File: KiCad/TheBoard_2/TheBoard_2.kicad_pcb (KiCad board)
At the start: 2 copper layers, 150 x 100 mm, 9 parts, among them J1 Conn_01x03_Female, J2 Conn_01x03_Female, J3 Conn_01x16_Female, J4 Conn_01x32_Male, J5 Conn_01x16_Female

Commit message: Adding ground to output pins
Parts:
- J4: value Conn_01x32_Male -> Conn_01x36_Male; footprint Connector_PinHeader_2.54mm:PinHeader_1x32_P2.54mm_Horizontal -> Connector_PinHeader_2.54mm:PinHeader_2x18_P2.54mm_Horizontal
- moved J4 19.8 mm to (176.5, 140.3)
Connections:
- J4 pad 1: unconnected-(J4-Pad1) -> GND
- J4 pad 2: unconnected-(J4-Pad2) -> GND

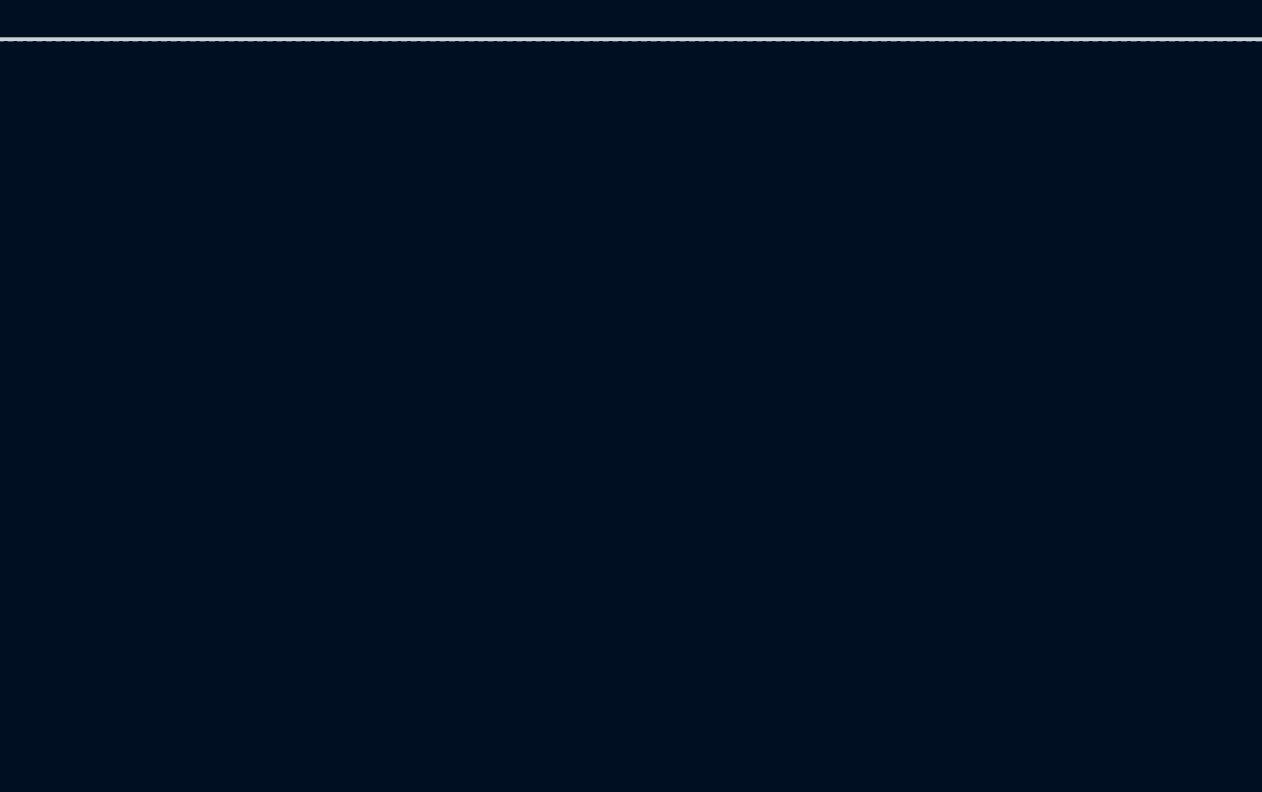
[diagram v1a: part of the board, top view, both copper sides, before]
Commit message: Adding -5V circuit
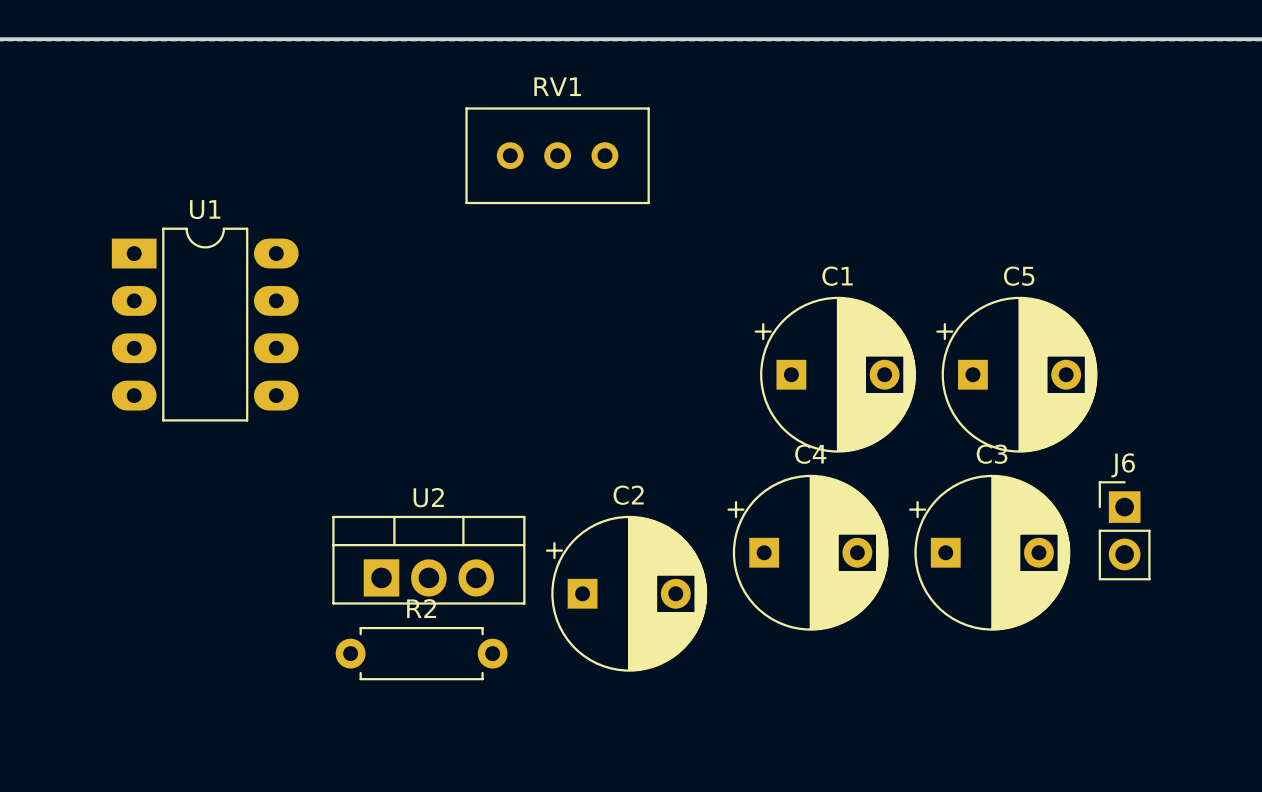
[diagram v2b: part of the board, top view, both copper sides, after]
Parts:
- added C1: C, Capacitor_THT:CP_Radial_D8.0mm_P5.00mm, F.Cu at (159.8, 65.2)
- added C2: C, Capacitor_THT:CP_Radial_D8.0mm_P5.00mm, F.Cu at (148.6, 77.0)
- added C3: C, Capacitor_THT:CP_Radial_D8.0mm_P5.00mm, F.Cu at (168.0, 74.8)
- added C4: C, Capacitor_THT:CP_Radial_D8.0mm_P5.00mm, F.Cu at (158.3, 74.8)
- added C5: C, Capacitor_THT:CP_Radial_D8.0mm_P5.00mm, F.Cu at (169.5, 65.2)
- added J6: Conn_01x02_Male, Connector_PinHeader_2.54mm:PinHeader_1x02_P2.54mm_Vertical, F.Cu at (177.6, 72.3)
- added R2: R, Resistor_THT:R_Axial_DIN0207_L6.3mm_D2.5mm_P7.62mm_Horizontal, F.Cu at (136.1, 80.2)
- added RV1: R_Potentiometer_Trim, Potentiometer_THT:Potentiometer_Bourns_3296W_Vertical, F.Cu at (149.8, 53.5)
- added U1: MAX680CSA+T, Package_DIP:DIP-8_W7.62mm_LongPads, F.Cu at (124.5, 58.8)
- added U2: LM337_TO220, Package_TO_SOT_THT:TO-220-3_Vertical, F.Cu at (137.8, 76.2)

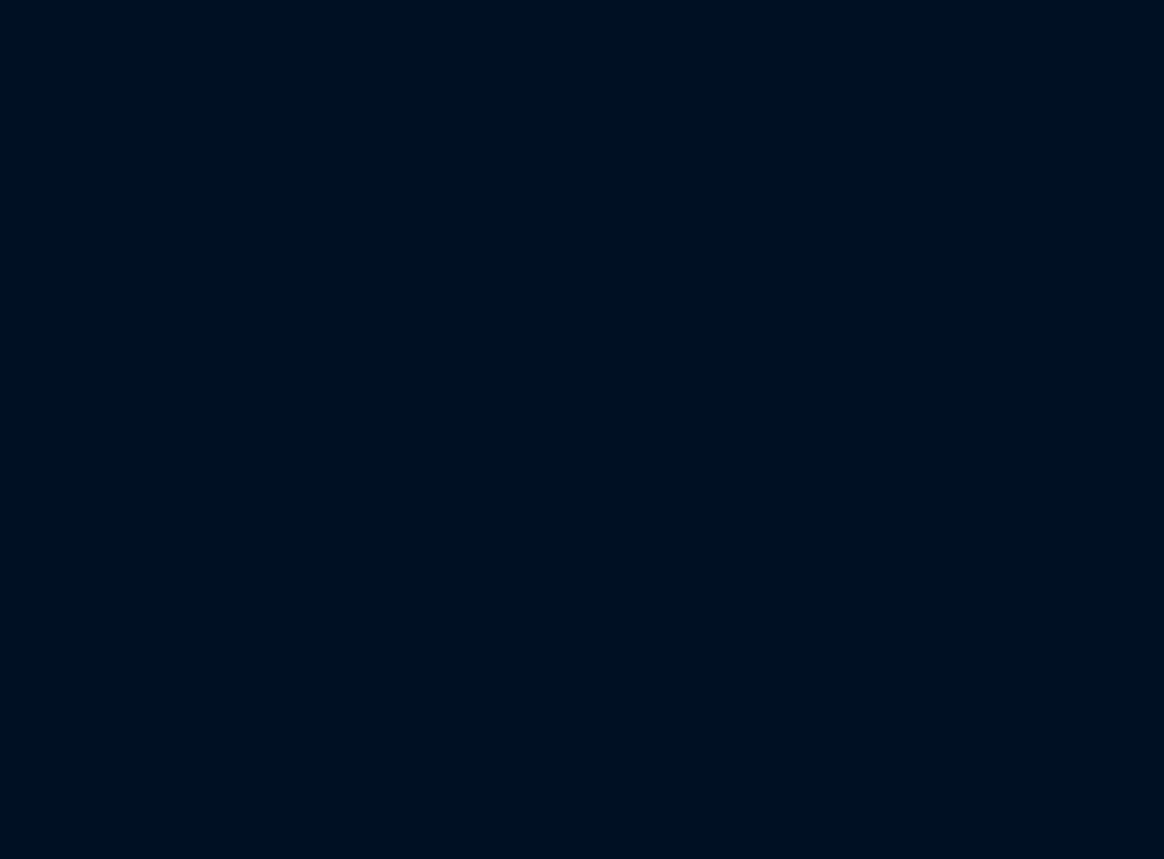
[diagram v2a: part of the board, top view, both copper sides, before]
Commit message: adding mt3608 circuit
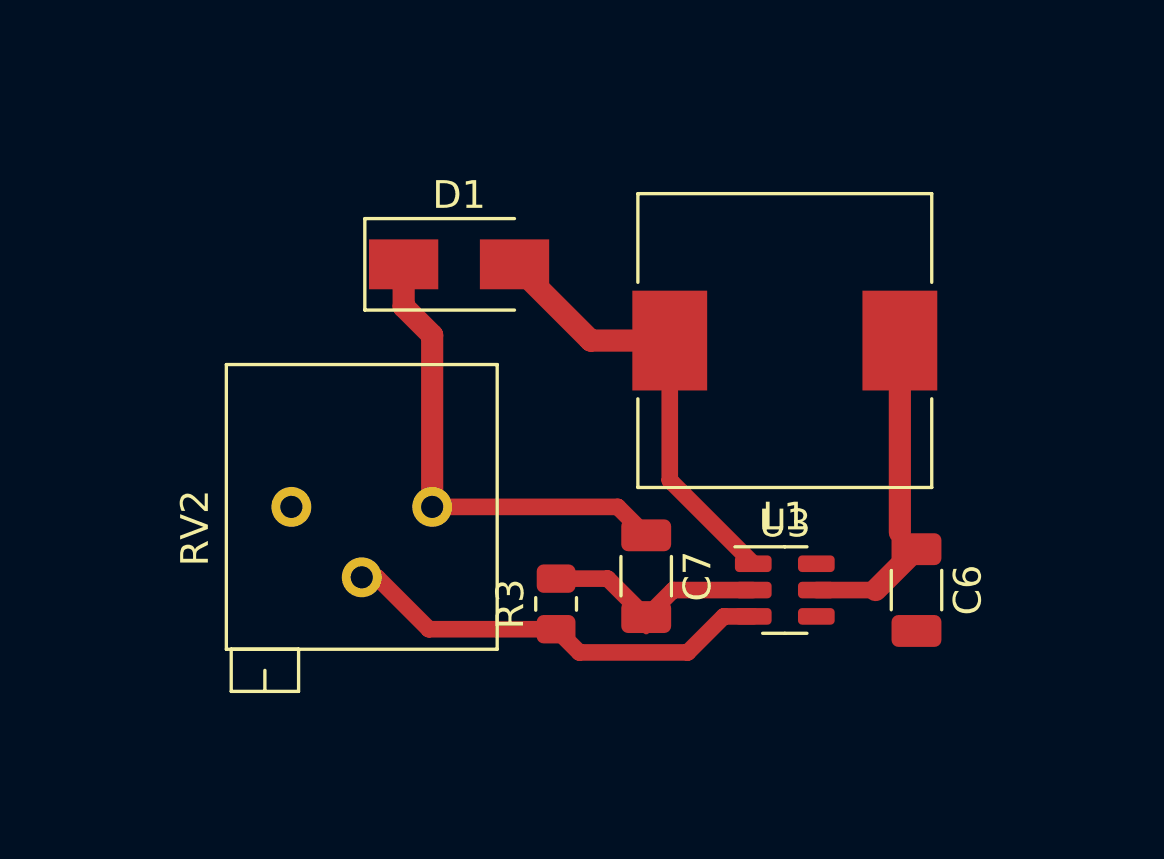
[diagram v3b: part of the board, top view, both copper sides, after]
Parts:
- added C6: C, Capacitor_SMD:C_1206_3216Metric, F.Cu at (134.0, 121.0)
- added C7: C, Capacitor_SMD:C_1206_3216Metric, F.Cu at (124.2, 120.5)
- added D1: D, Diode_SMD:D_SMA, F.Cu at (117.5, 109.2)
- added L1: L, Inductor_SMD:L_10.4x10.4_H4.8, F.Cu at (129.2, 112.0)
- added R3: R, Resistor_SMD:R_0805_2012Metric, F.Cu at (121.0, 121.5)
- added RV2: R_Potentiometer, Potentiometer_THT:Potentiometer_Bourns_3296P_Horizontal, F.Cu at (111.5, 118.0)
- added U3: MT3608, Package_TO_SOT_SMD:SOT-23-6, F.Cu at (129.2, 121.0)
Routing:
- net Net-(D1-Pad1): track 0.00 -> 17.3 mm
- net Net-(D1-Pad2): track 0.00 -> 16.0 mm
- net Net-(U3-Pad3): track 0.00 -> 15.8 mm
- net Net-(C6-Pad1): track 0.00 -> 12.0 mm
- net GND: track 0.00 -> 8.25 mm

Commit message: Adding battery circuit
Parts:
- added C10: C, Capacitor_SMD:C_0603_1608Metric_Pad1.08x0.95mm_HandSolder, F.Cu at (115.9, 112.3)
- added C8: C, Capacitor_SMD:C_0402_1005Metric_Pad0.74x0.62mm_HandSolder, F.Cu at (107.9, 114.1)
- added C9: C, Capacitor_SMD:C_0402_1005Metric_Pad0.74x0.62mm_HandSolder, F.Cu at (115.9, 108.4)
- added D2: LED, LED_SMD:LED_0402_1005Metric_Pad0.77x0.64mm_HandSolder, F.Cu at (110.7, 105.4)
- added D3: LED, LED_SMD:LED_0402_1005Metric_Pad0.77x0.64mm_HandSolder, F.Cu at (112.2, 105.4)
- added J7: USB_B_Micro, Connector_USB:USB_Micro-B_Molex_47346-0001, F.Cu at (102.4, 111.6)
- added Q1: FS8205A, Package_SO:TSSOP-8_4.4x3mm_P0.65mm, F.Cu at (120.7, 115.3)
- added R1: R, Resistor_SMD:R_0402_1005Metric_Pad0.72x0.64mm_HandSolder, F.Cu at (110.7, 107.9)
- added R4: R, Resistor_SMD:R_0402_1005Metric_Pad0.72x0.64mm_HandSolder, F.Cu at (112.2, 107.9)
- added R5: R, Resistor_SMD:R_0402_1005Metric_Pad0.72x0.64mm_HandSolder, F.Cu at (110.4, 118.6)
- added R6: R, Resistor_SMD:R_0402_1005Metric_Pad0.72x0.64mm_HandSolder, F.Cu at (115.9, 116.1)
- added R7: R, Resistor_SMD:R_0402_1005Metric_Pad0.72x0.64mm_HandSolder, F.Cu at (115.9, 105.8)
- added U4: TP4056, Package_SO:SOIC-8-1EP_3.9x4.9mm_P1.27mm_EP2.29x3mm, F.Cu at (111.7, 114.1)
- added U5: DW01, Package_TO_SOT_SMD:SOT-23-6_Handsoldering, F.Cu at (120.7, 108.1)
- moved C1 27.0 mm to (186.7, 64.5)
- moved C2 27.0 mm to (175.5, 76.2)
- moved C3 27.0 mm to (195.0, 74.0)
- moved C4 27.0 mm to (185.3, 74.0)
- moved C5 27.0 mm to (196.5, 64.5)
- moved J6 27.0 mm to (204.6, 71.5)
- moved R2 27.0 mm to (163.1, 79.4)
- moved RV1 27.0 mm to (176.7, 52.7)
- moved U1 27.0 mm to (151.5, 58.0)
- moved U2 27.0 mm to (164.7, 75.3)
- moved C6 19.5 mm to (153.2, 117.2)
- moved C7 19.5 mm to (143.4, 116.7)
- moved D1 19.5 mm to (136.7, 105.5)
- moved L1 19.5 mm to (148.4, 108.2)
- moved R3 19.5 mm to (140.2, 117.7)
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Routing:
- net GND: track 8.25 -> 41.3 mm
- net Net-(C8-Pad1): track 0.00 -> 29.5 mm, vias 0 -> 2
- net B-: track 0.00 -> 15.1 mm
- net unconnected-(J7-Pad6): track 0.00 -> 12.6 mm
- net OUT/B+: track 0.00 -> 10.7 mm
- net Net-(U5-Pad3): track 0.00 -> 9.62 mm, vias 0 -> 2
- net Net-(U5-Pad2): track 0.00 -> 8.22 mm, vias 0 -> 2
- net Net-(C9-Pad1): track 0.00 -> 8.12 mm
- net Net-(Q1-Pad1): track 0.00 -> 5.74 mm
- net Net-(R1-Pad2): track 0.00 -> 3.23 mm
- net Net-(R4-Pad2): track 0.00 -> 3.14 mm
- net Net-(U5-Pad1): track 0.00 -> 3.05 mm
- net Net-(R5-Pad1): track 0.00 -> 2.03 mm
- net Net-(D3-Pad1): track 0.00 -> 1.33 mm
- net Net-(D2-Pad1): track 0.00 -> 1.33 mm

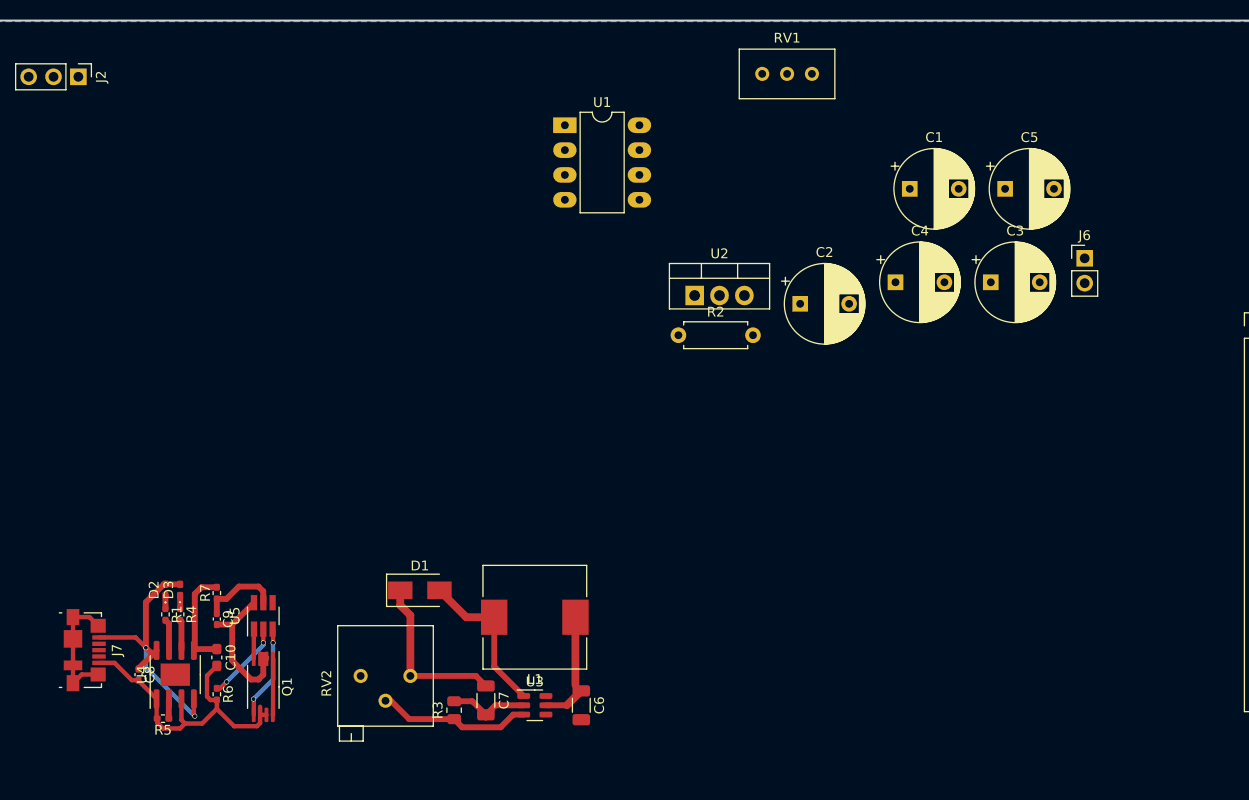
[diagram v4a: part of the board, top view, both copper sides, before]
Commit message: -5 generator circuit
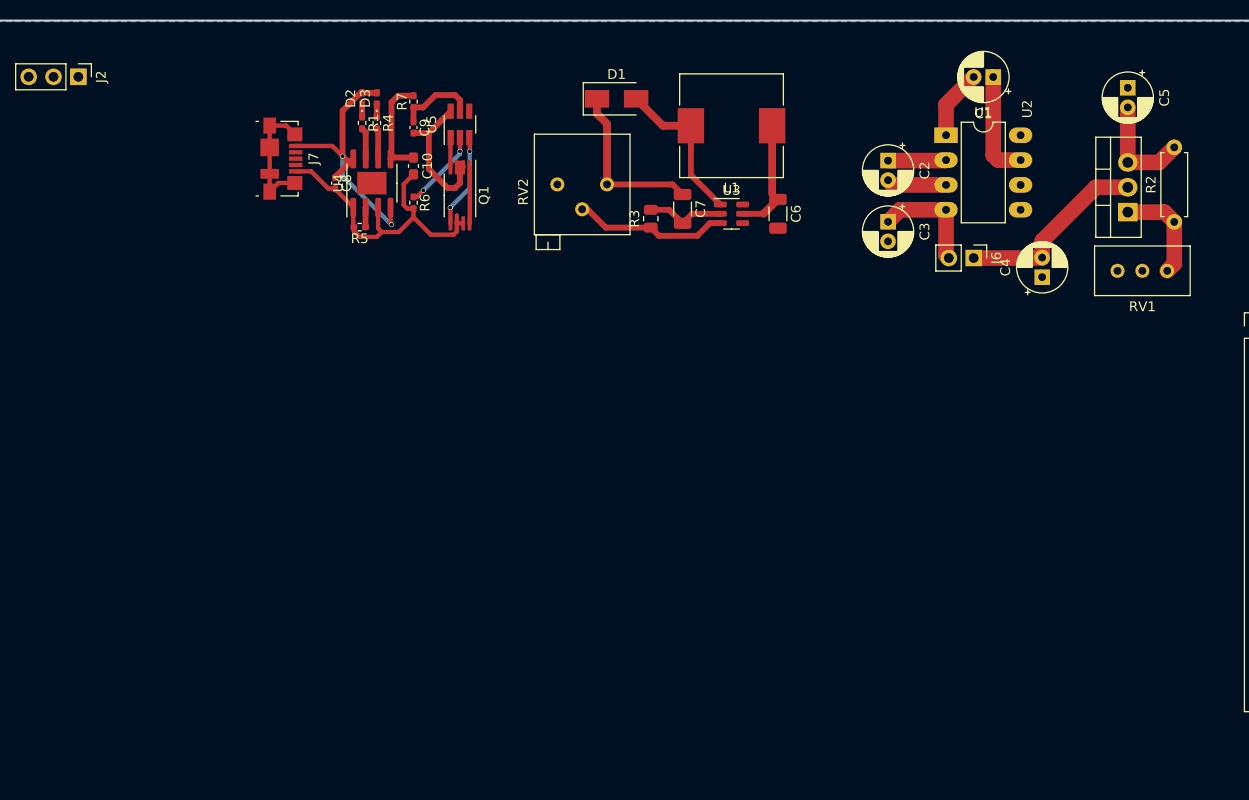
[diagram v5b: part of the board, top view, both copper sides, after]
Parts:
- C1, C2, C3, C4, C5: footprint Capacitor_THT:CP_Radial_D8.0mm_P5.00mm -> Capacitor_THT:CP_Radial_D5.0mm_P2.00mm
- moved C6 54.1 mm to (173.2, 67.0)
- moved C7 54.1 mm to (163.5, 66.5)
- moved D1 54.1 mm to (156.8, 55.2)
- moved L1 54.1 mm to (168.5, 58.0)
- moved Q1 54.1 mm to (140.8, 65.1)
- moved R3 54.1 mm to (160.2, 67.5)
- moved R5 54.1 mm to (130.5, 68.4)
- moved R6 54.1 mm to (136.0, 65.9)
- moved R7 54.1 mm to (136.0, 55.5)
- moved RV2 54.1 mm to (150.7, 64.0)
- moved U3 54.1 mm to (168.5, 67.0)
- moved C10 54.1 mm to (136.0, 62.1)
- moved C8 54.1 mm to (128.0, 63.9)
- moved C9 54.1 mm to (136.0, 58.2)
- moved D2 54.1 mm to (130.8, 55.2)
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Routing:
- net Net-(C4-Pad2): track 0.00 -> 19.7 mm
- net Net-(C3-Pad1): track 0.00 -> 11.5 mm
- net -5V: track 0.00 -> 11.0 mm
- net Net-(C1-Pad1): track 0.00 -> 11.0 mm
- net Net-(R2-Pad1): track 0.00 -> 10.5 mm
- net Net-(C1-Pad2): track 0.00 -> 7.12 mm
- net Net-(C2-Pad2): track 0.00 -> 6.13 mm
- net Net-(C2-Pad1): track 0.00 -> 5.95 mm

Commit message: added some output models
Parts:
- added U10: MCP6074-E/SL, Package_SO:SOIC-14_3.9x8.7mm_P1.27mm, F.Cu at (116.0, 94.2)
- added U11: MCP6074-E/SL, Package_SO:SOIC-14_3.9x8.7mm_P1.27mm, F.Cu at (132.9, 94.2)
- added U12: MCP6074-E/SL, Package_SO:SOIC-14_3.9x8.7mm_P1.27mm, F.Cu at (124.5, 94.2)
- added U13: MCP6074-E/SL, Package_SO:SOIC-14_3.9x8.7mm_P1.27mm, F.Cu at (107.5, 94.2)

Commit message: Adding rest of output opamps
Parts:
- added U6: MCP6074-E/SL, Package_SO:SOIC-14_3.9x8.7mm_P1.27mm, F.Cu at (116.2, 108.5)
- added U7: MCP6074-E/SL, Package_SO:SOIC-14_3.9x8.7mm_P1.27mm, F.Cu at (133.2, 108.5)
- added U8: MCP6074-E/SL, Package_SO:SOIC-14_3.9x8.7mm_P1.27mm, F.Cu at (124.7, 108.5)
- added U9: MCP6074-E/SL, Package_SO:SOIC-14_3.9x8.7mm_P1.27mm, F.Cu at (107.8, 108.5)
